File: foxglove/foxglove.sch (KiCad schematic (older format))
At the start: 50 parts, among them J1 NEIGHBOR1, J2 NEIGHBOR2, J3 Conn_02x05_Odd_Even, J4 Conn_02x05_Odd_Even, J5 Conn_01x02_Female, J7 BONUS_ROW, U1 ICE40HX8K-CT256, U2 TLV711, U3 MC4558CPT, U4 74LVC1G3157, U5 LM339, U6 ADP225, U7 DAC084S085, U8 74AHC1G04

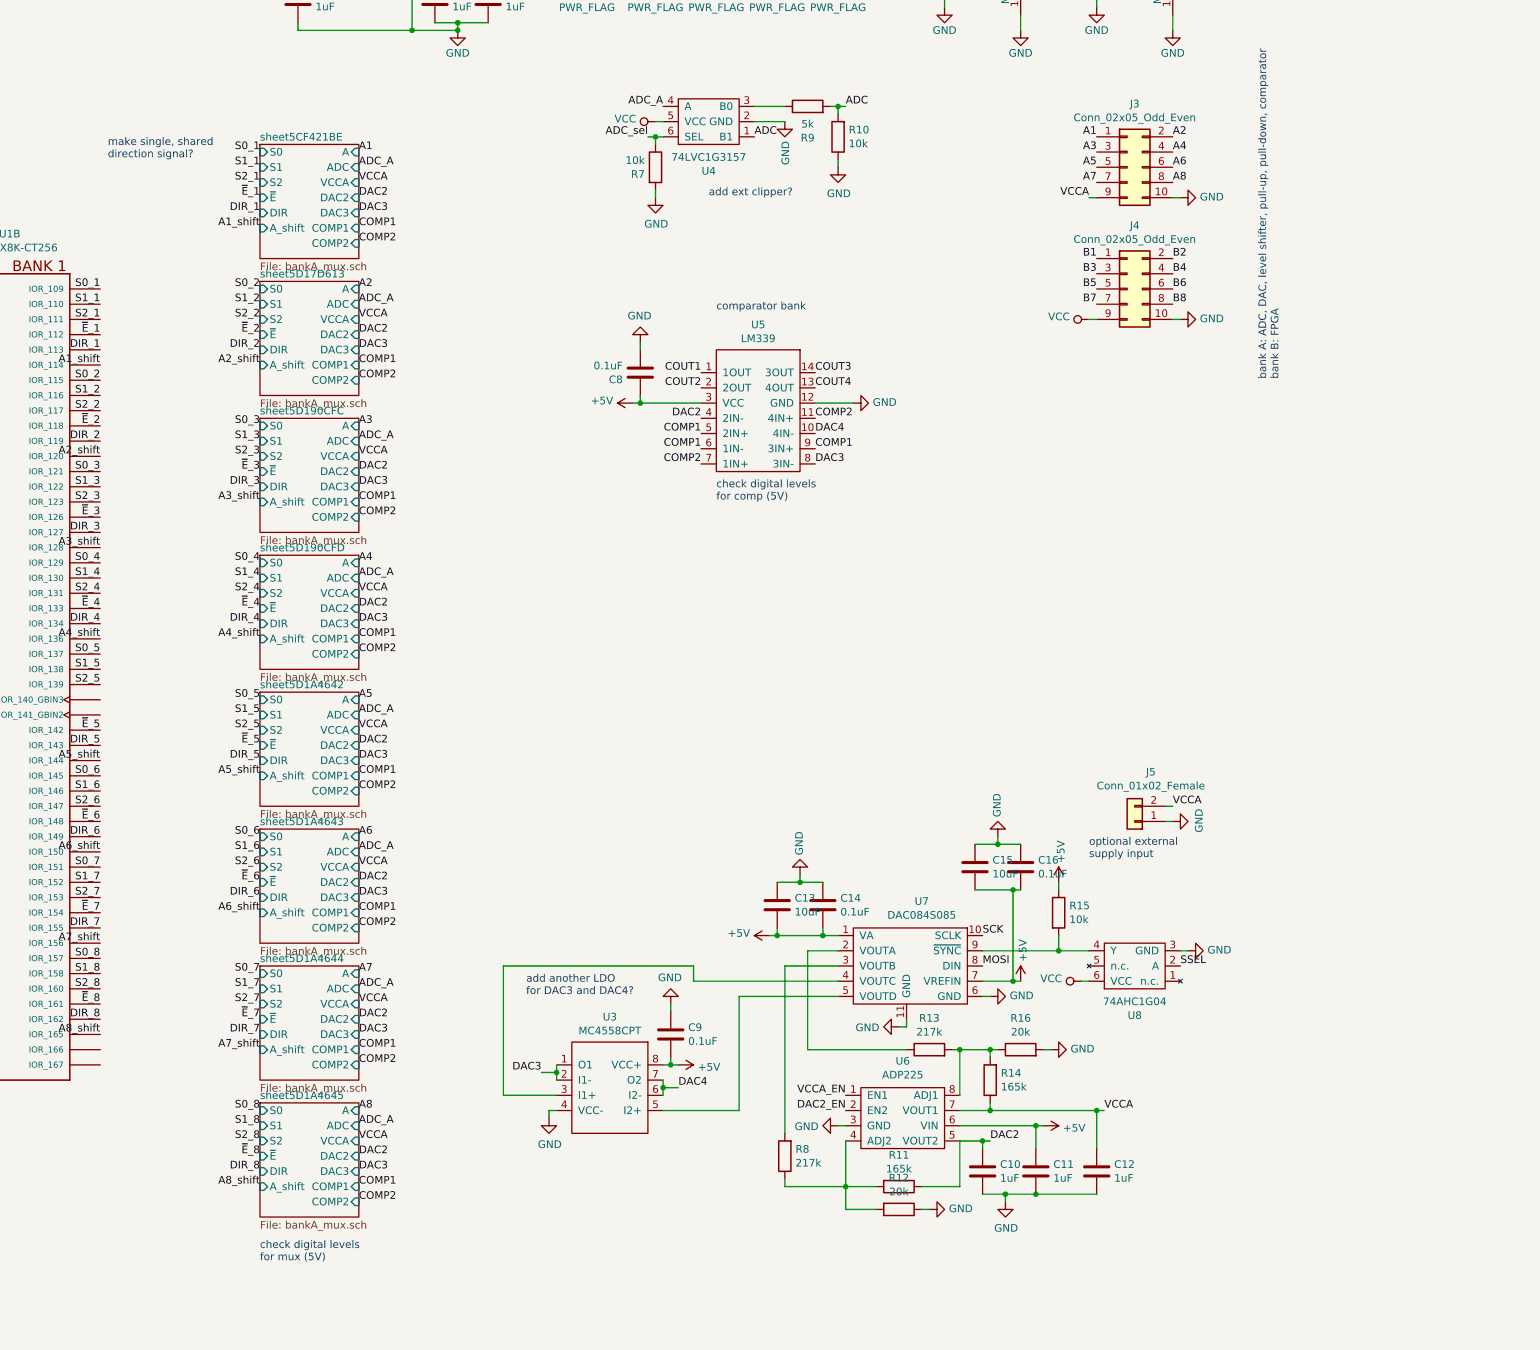
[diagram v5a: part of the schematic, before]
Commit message: Added design notes
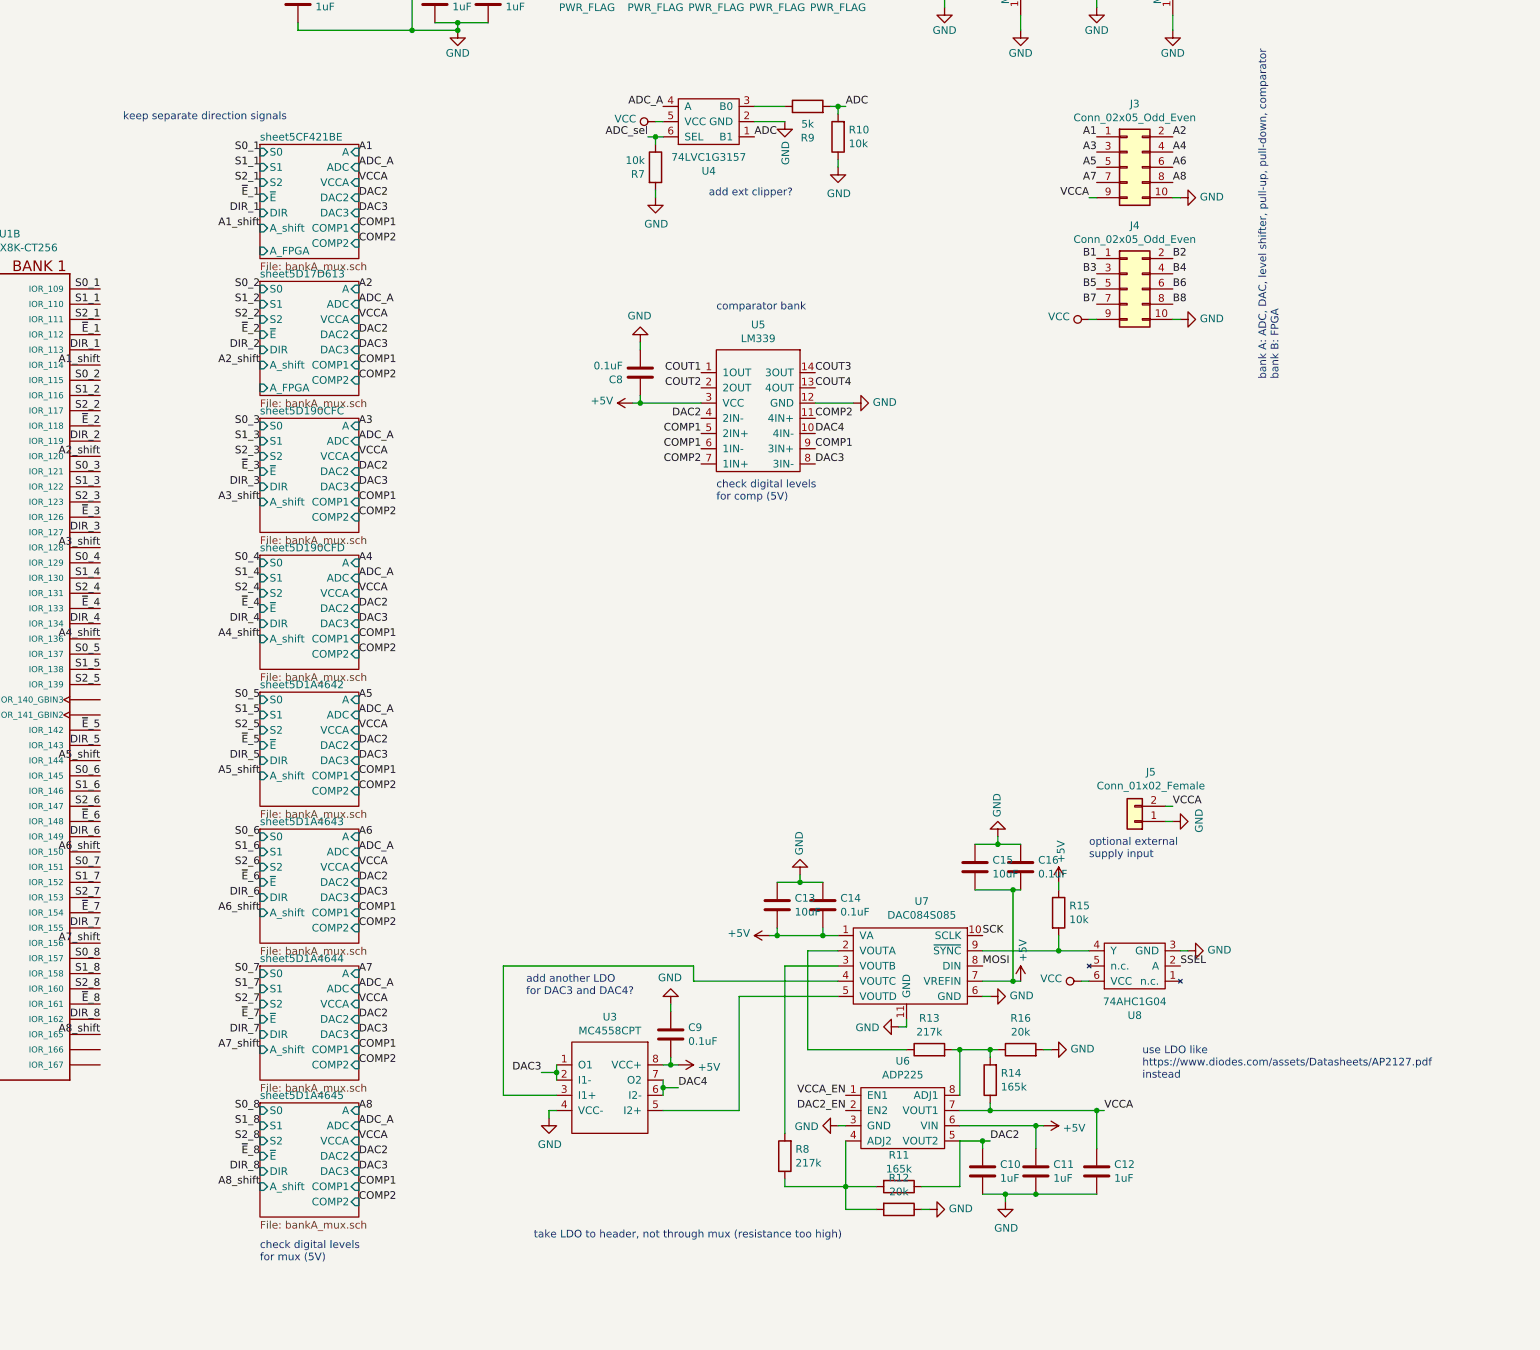
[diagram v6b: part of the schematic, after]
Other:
- note added: "keep separate direction signals"
- note added: "take LDO to header, not through mux (resistance too high)"
- note added: "use LDO like \nhttps://www.diodes.com/assets/Datasheets/AP2127.pdf\ninstead"
- note removed: "make single, shared\ndirection signal?"
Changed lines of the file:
@@
 F13 "COMP1" I R 10750 2550 50
 F14 "COMP2" I R 10750 2650 50
+F15 "A_FPGA" I L 10100 2700 50
 $EndSheet
 Text Notes 16800 3550 1    50   ~ 0
@@
 F13 "COMP1" I R 10750 3450 50
 F14 "COMP2" I R 10750 3550 50
+F15 "A_FPGA" I L 10100 3600 50
 $EndSheet
 Text Label 10750 3450 0    50   ~ 0
@@
 Wire Wire Line
 	1900 9150 1950 9150
-Text Notes 9100 2100 0    50   ~ 0
-make single, shared\ndirection signal?
+Text Notes 9200 1850 0    50   ~ 0
+keep separate direction signals
 Wire Bus Line
 	2600 1900 4600 1900
@@
 Wire Bus Line
 	3150 6800 6450 6800
+Text Notes 11900 9200 0    50   ~ 0
+take LDO to header, not through mux (resistance too high)
+Text Notes 15900 8150 0    50   ~ 0
+use LDO like \nhttps://www.diodes.com/assets/Datasheets/AP2127.pdf\ninstead
 $EndSCHEMATC

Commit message: added design notes
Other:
- note added: "need to compare between pins?"
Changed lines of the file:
@@
 Wire Bus Line
 	3150 6800 6450 6800
+Text Notes 11600 4200 0    50   ~ 0
+need to compare between pins?
 $EndSCHEMATC
